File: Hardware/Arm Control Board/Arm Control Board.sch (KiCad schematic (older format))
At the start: 29 parts

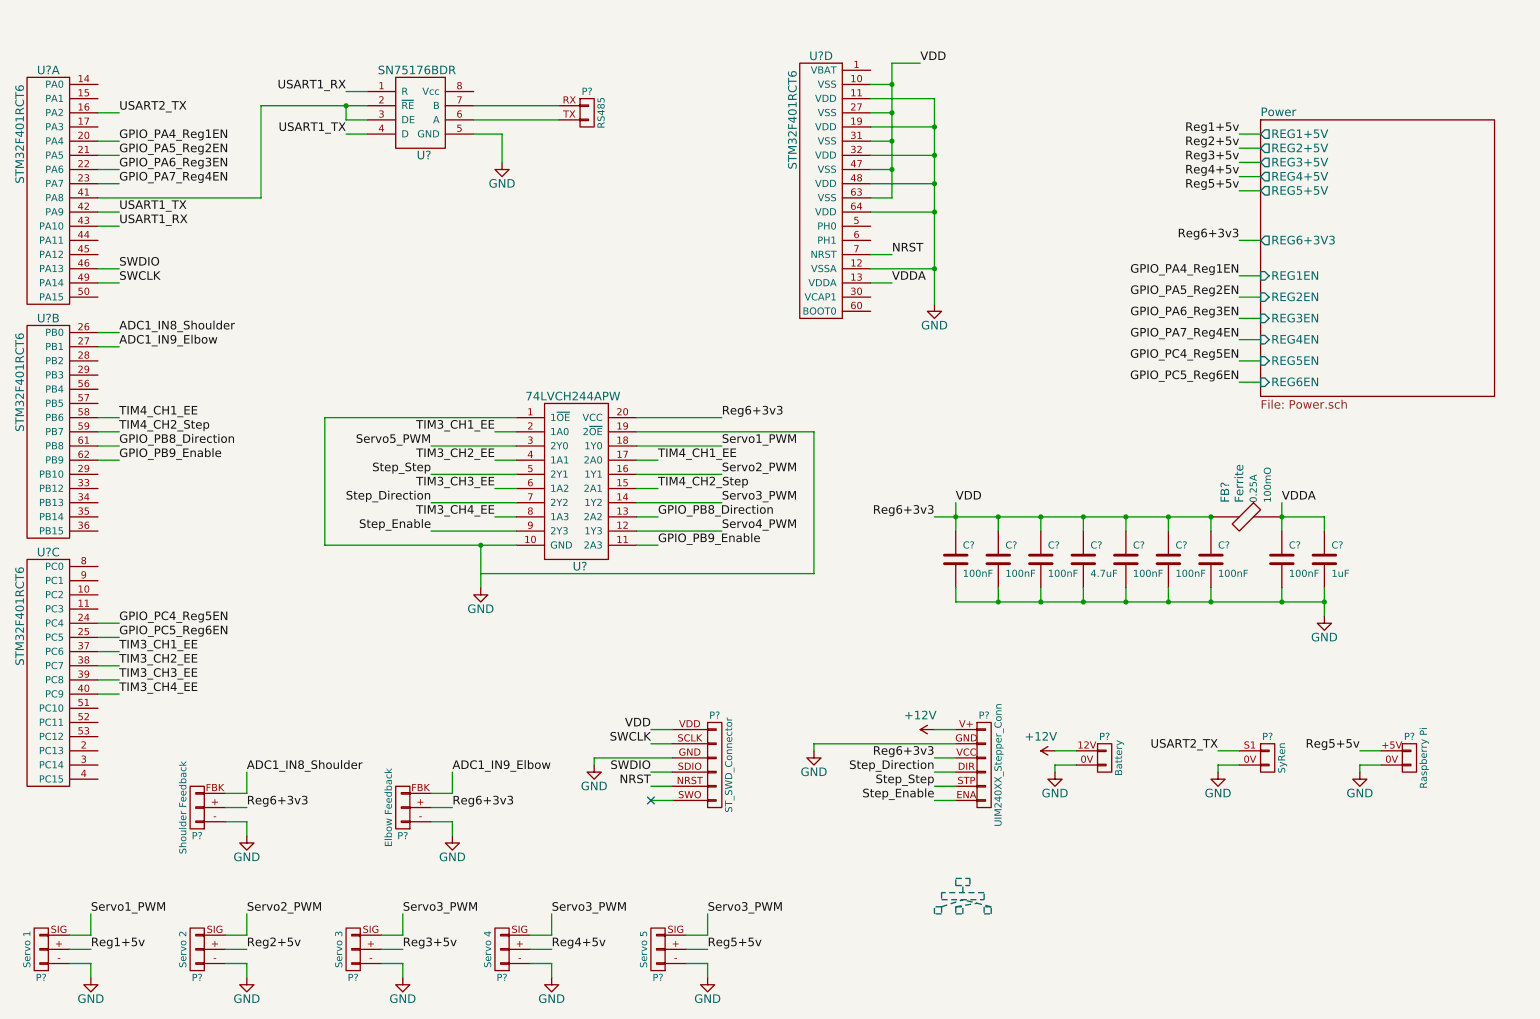
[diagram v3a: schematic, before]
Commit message: Fixed some floating wires
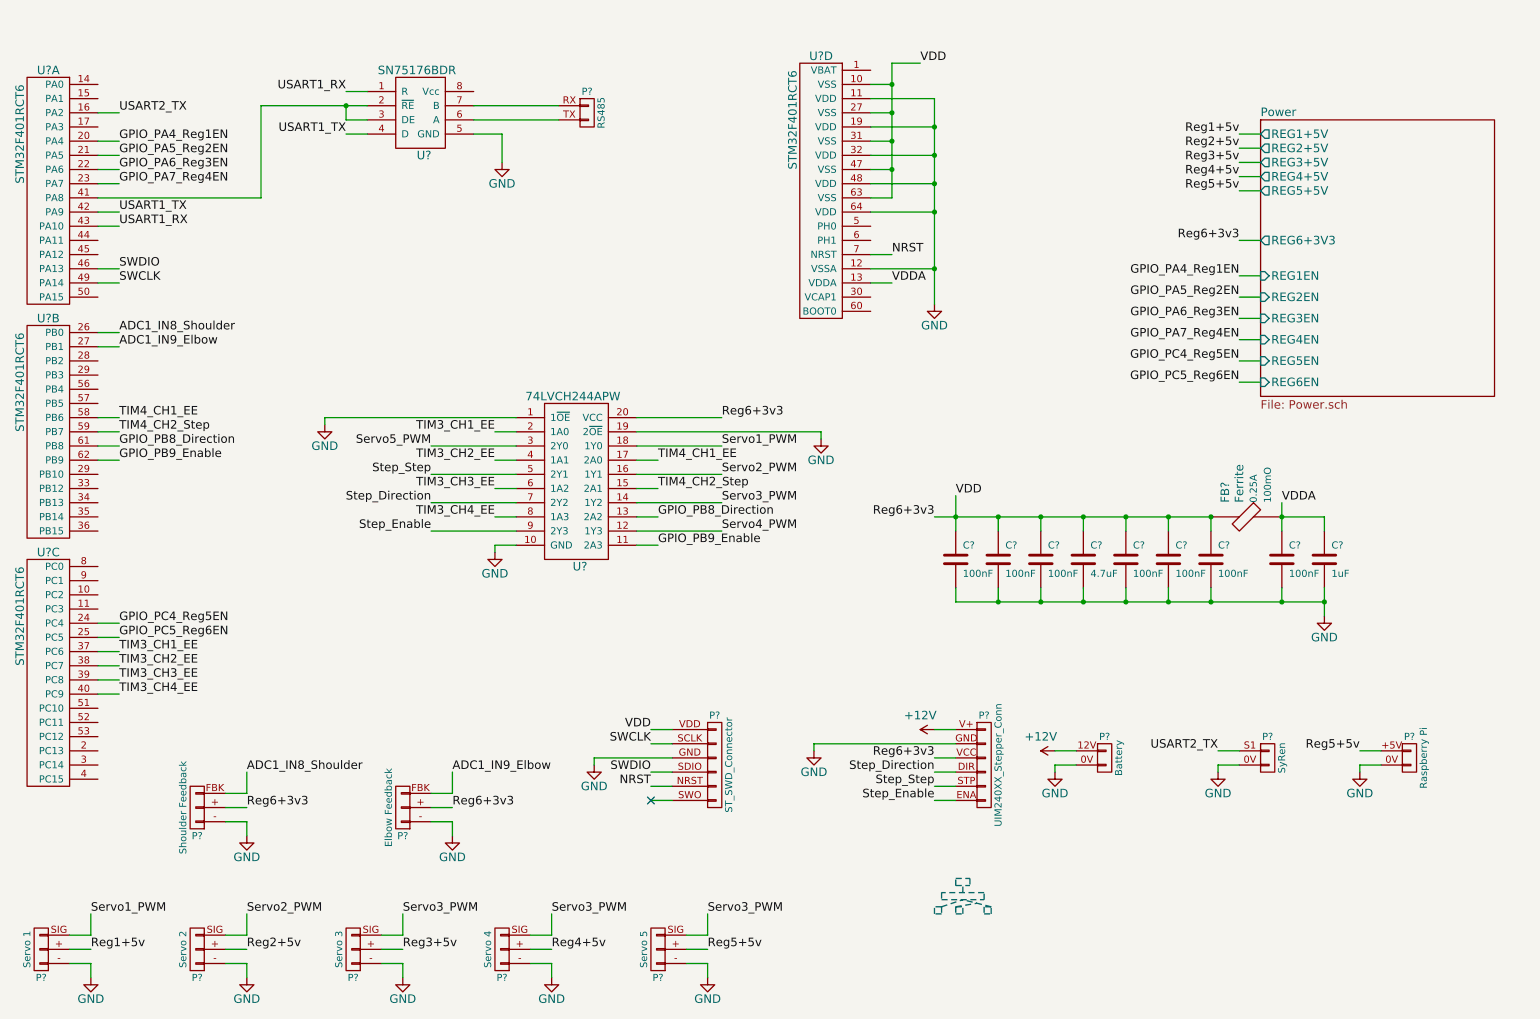
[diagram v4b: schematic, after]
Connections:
- net GND: now also U?.19 (2~OE)
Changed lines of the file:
@@
 L GND #PWR011
 U 1 1 54C88705
-P 3900 4600
-F 0 "#PWR011" H 3900 4350 60  0001 C CNN
-F 1 "GND" H 3900 4450 60  0000 C CNN
-F 2 "" H 3900 4600 60  0000 C CNN
-F 3 "" H 3900 4600 60  0000 C CNN
-	1    3900 4600
+P 4000 4350
+F 0 "#PWR011" H 4000 4100 60  0001 C CNN
+F 1 "GND" H 4000 4200 60  0000 C CNN
+F 2 "" H 4000 4350 60  0000 C CNN
+F 3 "" H 4000 4350 60  0000 C CNN
+	1    4000 4350
 	1    0    0    -1
 $EndComp
@@
 	1    0    0    -1
 $EndComp
-Text Label 7250 4000 0    60   ~ 0
+Text Label 7250 3950 0    60   ~ 0
 VDD
 Text Label 6800 2450 0    60   ~ 0
@@
 	2350 1850 1200 1850
 Wire Wire Line
-	2350 1200 3100 1200
+	2350 1200 2950 1200
+Wire Wire Line
+	2950 1200 3100 1200
 Wire Wire Line
 	9250 5850 9100 5850
@@
 	10100 5750 10250 5750
 Wire Wire Line
-	2800 4300 4150 4300
-Wire Wire Line
-	3900 4300 3900 4600
-Wire Wire Line
 	10250 5850 10100 5850
 Wire Wire Line
@@
 	2800 3400 4150 3400
 Wire Wire Line
-	5000 3500 6250 3500
+	5000 3500 6300 3500
 Wire Wire Line
 	6650 1150 7100 1150
 Wire Wire Line
-	7100 1150 7100 2600
+	7100 1150 7100 1350
+Wire Wire Line
+	7100 1350 7100 1550
+Wire Wire Line
+	7100 1550 7100 1750
+Wire Wire Line
+	7100 1750 7100 1950
+Wire Wire Line
+	7100 1950 7100 2350
+Wire Wire Line
+	7100 2350 7100 2600
 Wire Wire Line
 	6650 1950 7100 1950
@@
 	6800 1250 6650 1250
 Wire Wire Line
-	6800 900  6800 1850
+	6800 900  6800 1050
+Wire Wire Line
+	6800 1050 6800 1250
+Wire Wire Line
+	6800 1250 6800 1450
+Wire Wire Line
+	6800 1450 6800 1650
+Wire Wire Line
+	6800 1650 6800 1850
 Wire Wire Line
 	6800 900  7000 900
@@
 	9050 4100 9050 4200
 Wire Wire Line
-	7250 4000 7250 4200
+	7250 3950 7250 4100
+Wire Wire Line
+	7250 4100 7250 4200
 Connection ~ 7250 4100
 Wire Wire Line
@@
 Connection ~ 6800 1050
 Wire Wire Line
-	9550 4000 9550 4200
+	9550 4000 9550 4100
+Wire Wire Line
+	9550 4100 9550 4200
 Connection ~ 9050 4100
 Connection ~ 9550 4100
@@
 	9850 4100 9850 4200
 Wire Wire Line
-	9850 4600 9850 4800
+	9850 4600 9850 4700
+Wire Wire Line
+	9850 4700 9850 4800
 Wire Wire Line
 	9550 4700 9550 4600
@@
 	9550 4100 9850 4100
 Wire Wire Line
-	7250 4700 9850 4700
-Wire Wire Line
-	7100 4100 9050 4100
+	7250 4700 7550 4700
+Wire Wire Line
+	7550 4700 7850 4700
+Wire Wire Line
+	7850 4700 8150 4700
+Wire Wire Line
+	8150 4700 8450 4700
+Wire Wire Line
+	8450 4700 8750 4700
+Wire Wire Line
+	8750 4700 9050 4700
+Wire Wire Line
+	9050 4700 9550 4700
+Wire Wire Line
+	9550 4700 9850 4700
+Wire Wire Line
+	7100 4100 7250 4100
+Wire Wire Line
+	7250 4100 7550 4100
+Wire Wire Line
+	7550 4100 7850 4100
+Wire Wire Line
+	7850 4100 8150 4100
+Wire Wire Line
+	8150 4100 8450 4100
+Wire Wire Line
+	8450 4100 8750 4100
+Wire Wire Line
+	8750 4100 9050 4100
 Wire Wire Line
 	9400 1400 9250 1400
@@
 Text Label 3550 3600 2    60   ~ 0
 Servo5_PWM
-Wire Wire Line
-	6250 3500 6250 4500
-Wire Wire Line
-	6250 4500 3900 4500
-Wire Wire Line
-	2800 3400 2800 4300
-Connection ~ 3900 4300
 Wire Wire Line
 	7950 5850 7950 5900
@@
 Text Label 5100 5600 2    60   ~ 0
 VDD
+Wire Wire Line
+	6300 3500 6300 3550
+$Comp
+L GND #PWR?
+U 1 1 54CA4C25
+P 6300 3550
+F 0 "#PWR?" H 6300 3300 60  0001 C CNN
+F 1 "GND" H 6300 3400 60  0000 C CNN
+F 2 "" H 6300 3550 60  0000 C CNN
+F 3 "" H 6300 3550 60  0000 C CNN
+	1    6300 3550
+	1    0    0    -1
+$EndComp
+Wire Wire Line
+	2800 3400 2800 3450
+$Comp
+L GND #PWR?
+U 1 1 54CA5327
+P 2800 3450
+F 0 "#PWR?" H 2800 3200 60  0001 C CNN
+F 1 "GND" H 2800 3300 60  0000 C CNN
+F 2 "" H 2800 3450 60  0000 C CNN
+F 3 "" H 2800 3450 60  0000 C CNN
+	1    2800 3450
+	1    0    0    -1
+$EndComp
+Wire Wire Line
+	4000 4350 4000 4300
+Wire Wire Line
+	4000 4300 4150 4300
 $EndSCHEMATC

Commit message: Reorganized regulators, added 5V reg, ext osc, PNs
Way too much for one commit, sorry about that. Reorganized the
regulators into high voltage/low voltage sheets. Added product numbers
to all passives + more. Check issues for any other changes
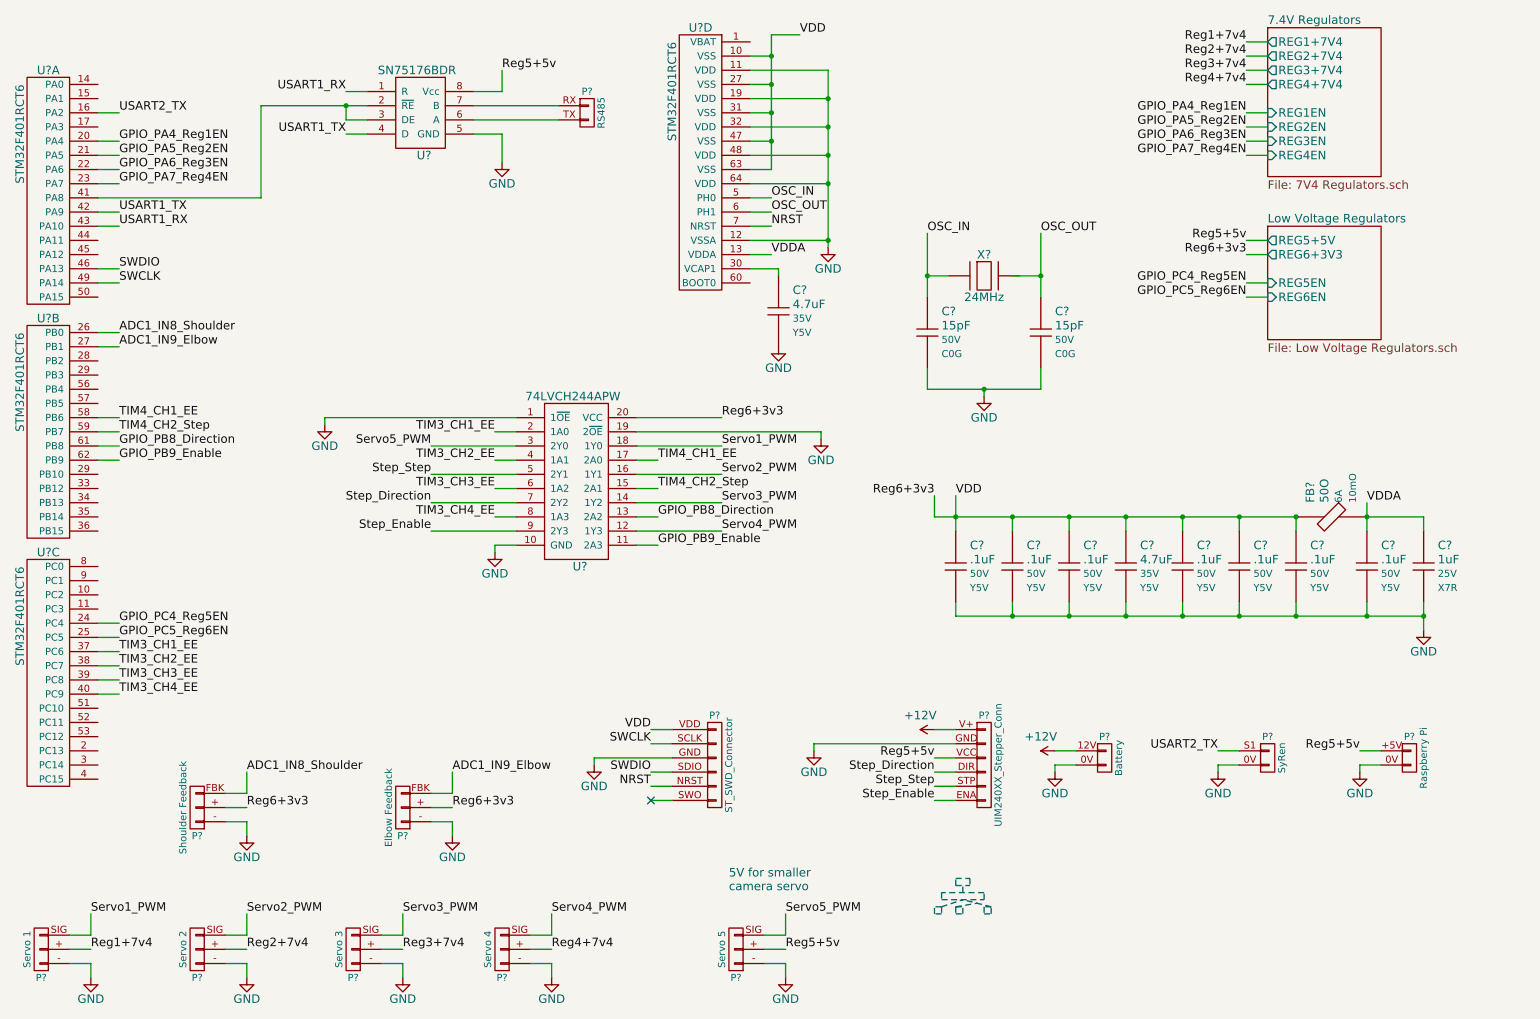
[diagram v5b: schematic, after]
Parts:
- removed C? (x7): 100nF, symbol C
- removed C?: 4.7uF, symbol C
- removed C?: 1uF, symbol C
- added C? (x7): .1uF, Capacitors_SMD:C_1206_HandSoldering, symbol Capacitor
- added C? (x2): 4.7uF, Capacitors_SMD:C_1206_HandSoldering, symbol Capacitor
- added C?: 1uF, Capacitors_SMD:C_1206_HandSoldering, symbol Capacitor
- added C? (x2): 15pF, symbol Capacitor
- added X?: 24MHz, Crystals_Oscillators_SMD:Q_49U3HMS, symbol Crystal
- FB?: value Ferrite -> 50O; footprint (none) -> Resistors_SMD:R_1206_HandSoldering; Current 0.25A -> 6A; DCR 100mO -> 10mO; Manufacturer Value -> Laird-Signal; Manufacturer Part # Value -> HI1206T500R-10; Vendor Value -> Digi-Key; Vendor Part # Value -> 240-2412-1-ND
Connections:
- net GND: now also C?.2, C?.2, C?.2, C?.2, C?.2, C?.2, C?.2, C?.2, C?.2, C?.2, C?.2, C?.2
- net Reg5+5v: now also P?.VCC, U?.8 (Vcc)
- net Reg6+3v3: now also C?.1, C?.1, C?.1, C?.1, C?.1, C?.1, C?.1; no longer P?.VCC
- net Servo3_PWM: no longer P?.SIG, P?.SIG
- net Servo4_PWM: now also P?.SIG
- net Servo5_PWM: now also P?.SIG
- net VDDA: now also C?.1, C?.1
- net at U?.30 (VCAP1): now also C?.1
- net OSC_IN: now reaches U?.5 (PH0)
- net OSC_IN: now also C?.1, X?.1
- net OSC_OUT: now reaches U?.6 (PH1)
- net OSC_OUT: now also C?.1
- net Reg1+5v renamed Reg1+7v4
- net Reg2+5v renamed Reg2+7v4
- net Reg3+5v renamed Reg3+7v4
- net Reg4+5v renamed Reg4+7v4
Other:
- note added: "5V for smaller \ncamera servo"
- moved on the sheet: FB?, P?, U?D

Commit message: More footprints added, components annotated
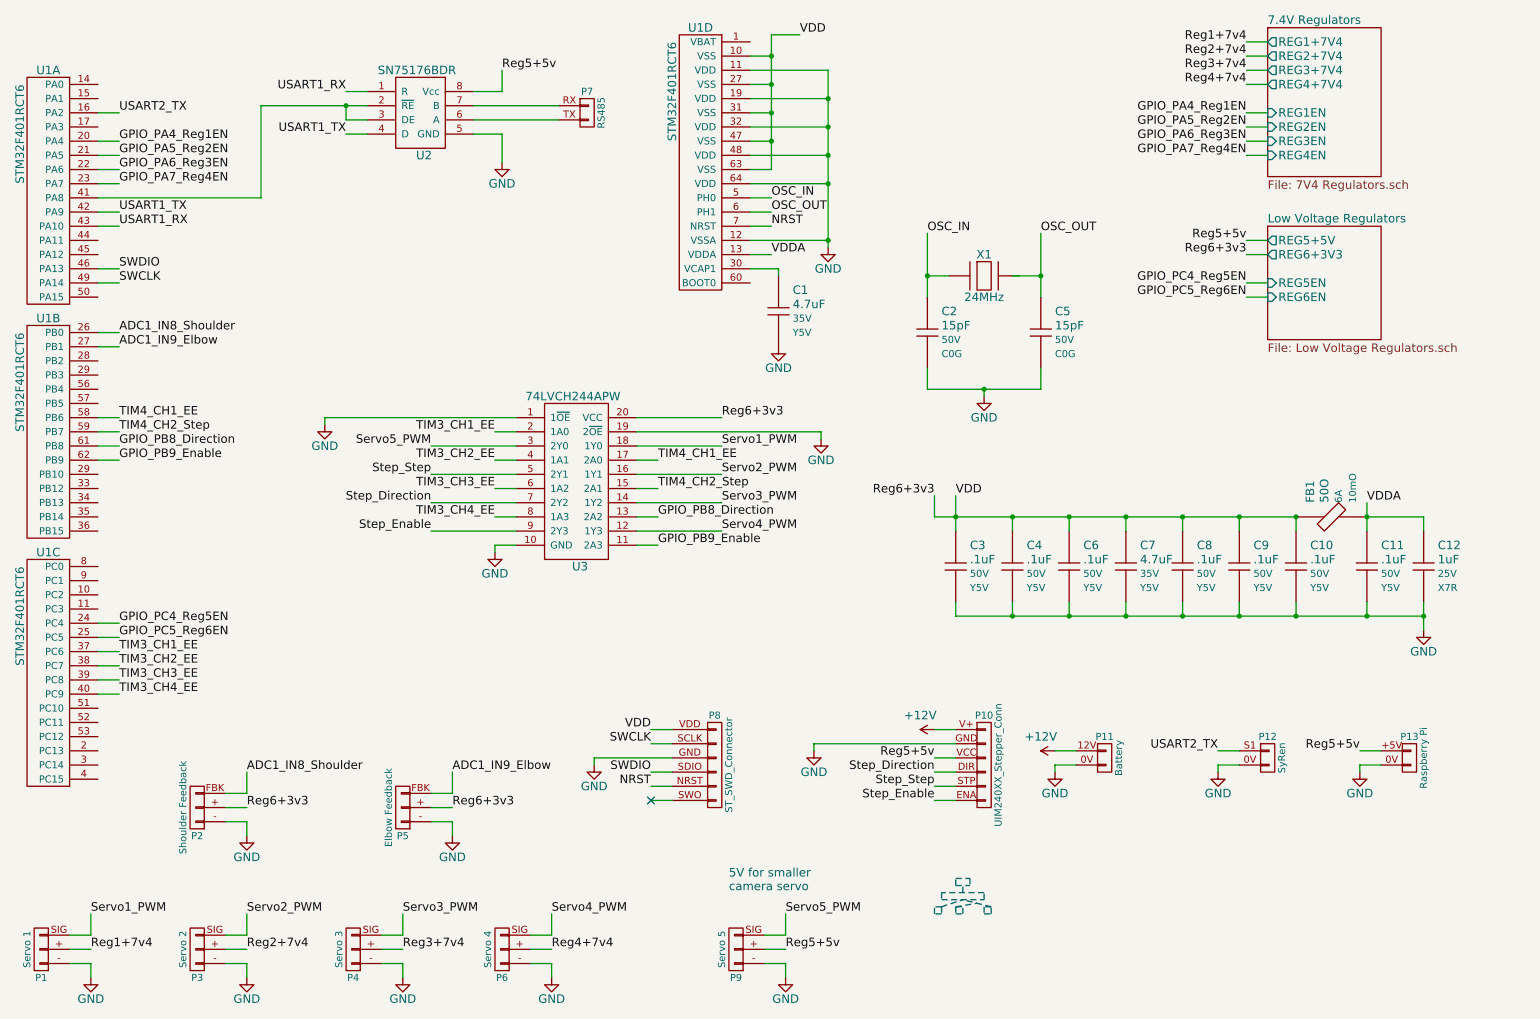
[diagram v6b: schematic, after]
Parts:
- U1: renamed from U?; footprint (none) -> Housings_QFP:LQFP-64_10x10mm_Pitch0.5mm
- U2: renamed from U?; footprint (none) -> SMD_Packages:SOIC-8-W
- U3: renamed from U?; footprint (none) -> MAVRIC_footprints:AB2_TSSOP20
- gave numbers to parts that had none: 28

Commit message: Initial PCB layout
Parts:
- C2, C5: footprint (none) -> Capacitors_SMD:C_1206_HandSoldering
- U1: footprint (none) -> Housings_QFP:LQFP-64_10x10mm_Pitch0.5mm
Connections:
- net GND: now also U1.10 (VSS), U1.27 (VSS), U1.31 (VSS), U1.47 (VSS), U1.63 (VSS); no longer U1.11 (VDD), U1.12 (VSSA), U1.19 (VDD), U1.32 (VDD), U1.48 (VDD), U1.64 (VDD)
- net OSC_OUT: now also X1.2
- net Reg6+3v3: now also U1.11 (VDD), U1.12 (VSSA), U1.19 (VDD), U1.32 (VDD), U1.48 (VDD), U1.64 (VDD); no longer U1.10 (VSS), U1.27 (VSS), U1.31 (VSS), U1.47 (VSS), U1.63 (VSS)
- no-connect marks 1 -> 28
